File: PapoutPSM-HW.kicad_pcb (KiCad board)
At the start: 2 copper layers, 80 x 50 mm, 96 parts, among them J1 53015-0510, J2 Barrel_Jack, J3 53015-0510, Q1 2N7002, Q2 2N7002, Q3 2N7002, SW1 DSIC04LSGET, U1 LMR14020SDDA, U10 SP3232EEY-L, U2 78L05G-AB3-R, U3 EL3H7-G, U4 EL3H7-G, U5 EL3H7-G, U6 EL3H7-G, U7 EL3H7-G, U8 EL3H7-G, U9 MSP430FR2433IRGE

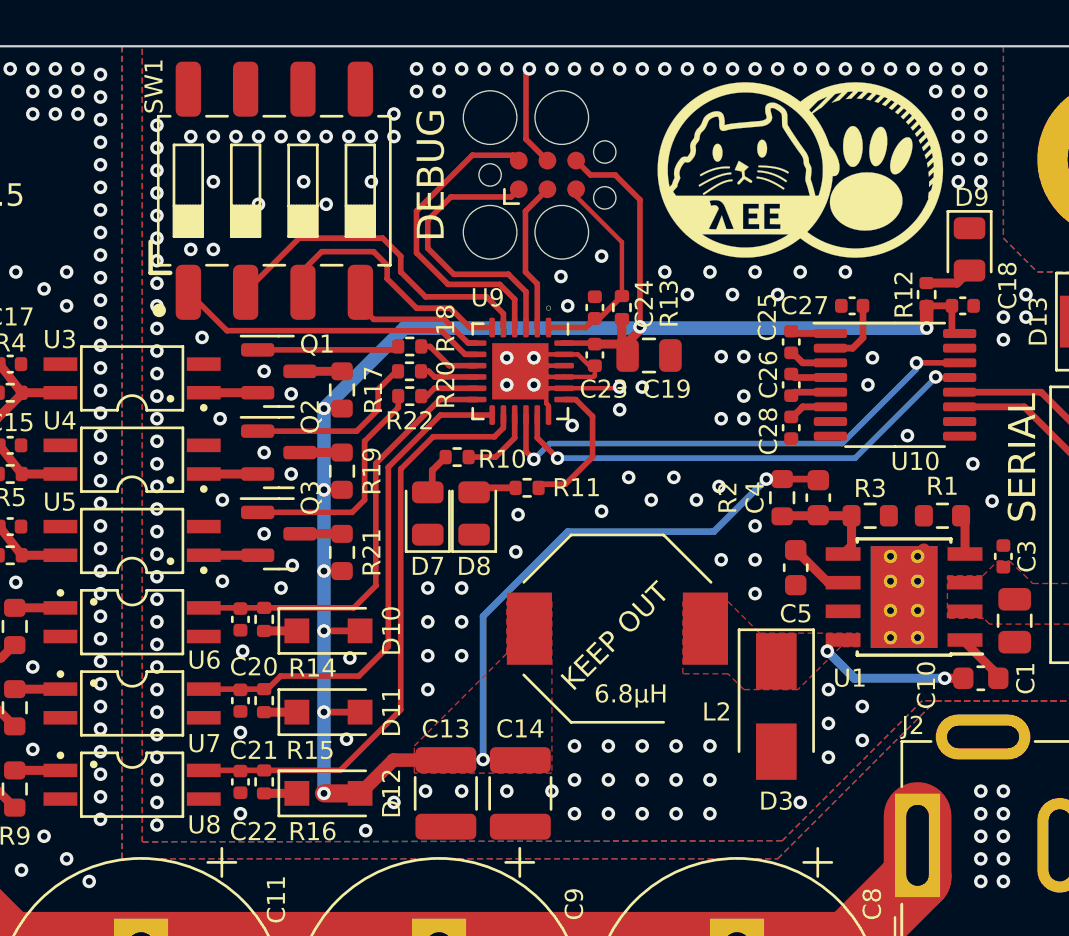
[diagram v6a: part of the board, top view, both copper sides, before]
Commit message: Update latest changes on low-side NMos usage
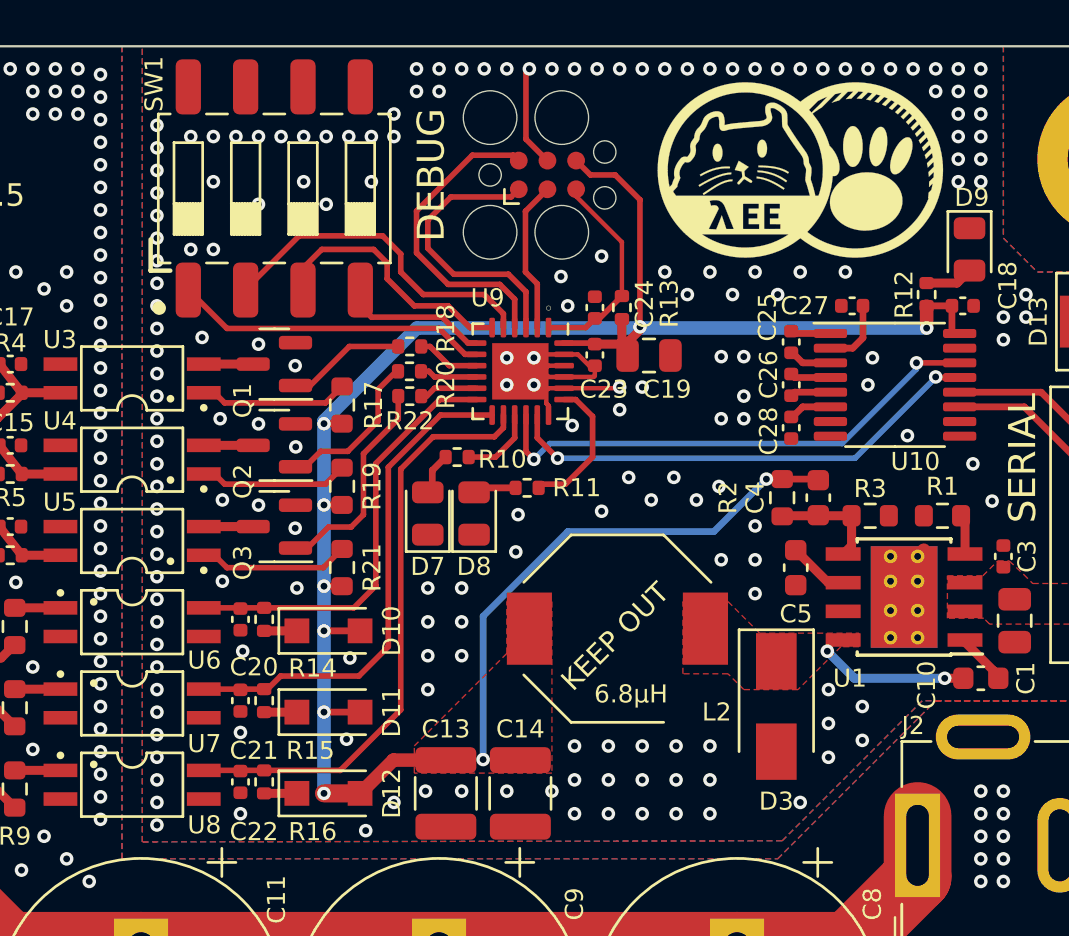
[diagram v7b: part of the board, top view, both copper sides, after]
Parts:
- moved R17 0.67 mm to (85.7, 65.9)
- moved R19 0.67 mm to (85.7, 69.5)
- moved R21 0.67 mm to (85.7, 73.1)
- moved Q1 0.38 mm to (82.7, 64.1), turned to 180 degrees
- moved Q2 0.38 mm to (82.7, 67.7), turned to 180 degrees
- moved Q3 0.38 mm to (82.7, 71.3), turned to 180 degrees
- moved SW1 0.10 mm to (82.7, 56.3)
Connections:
- Q1 pad 2: /ANODE_INHIBIT -> GND
- Q1 pad 3: Net-(Q1-Pad3) -> /CATHODE_INHIBIT
- Q2 pad 2: /ANODE_RESET -> GND
- Q2 pad 3: Net-(Q2-Pad3) -> /CATHODE_RESET
- Q3 pad 2: /ANODE_PULSE -> GND
- Q3 pad 3: Net-(Q3-Pad3) -> /CATHODE_PULSE
- R17 pad 1: Net-(Q1-Pad3) -> /ANODE_INHIBIT
- R19 pad 1: Net-(Q2-Pad3) -> /ANODE_RESET
- R21 pad 1: Net-(Q3-Pad3) -> /ANODE_PULSE
- U3 pad 2: GND -> /CATHODE_INHIBIT
- U4 pad 2: GND -> /CATHODE_RESET
- U5 pad 2: GND -> /CATHODE_PULSE
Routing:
- net /ANODE_PULSE: track 2.39 -> 6.70 mm
- net /ANODE_RESET: track 2.39 -> 6.61 mm
- net /ANODE_INHIBIT: track 2.39 -> 6.61 mm
- net /CATHODE_RESET: track 0.00 -> 2.39 mm
- net /CATHODE_PULSE: track 0.00 -> 2.39 mm
- net /CATHODE_INHIBIT: track 0.00 -> 2.39 mm
- net Net-(Q3-Pad3): track 1.86 -> 0.00 mm
- net Net-(Q2-Pad3): track 1.86 -> 0.00 mm
- net Net-(Q1-Pad3): track 1.86 -> 0.00 mm
- net Net-(Q1-Pad1): track 6.50 -> 5.07 mm
- net Net-(Q2-Pad1): track 7.84 -> 6.91 mm
- net Net-(Q3-Pad1): track 10.2 -> 9.31 mm
